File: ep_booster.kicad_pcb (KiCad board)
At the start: 2 copper layers, 45 x 21.2 mm, 31 parts, among them J1 TB002-500-04BE, J2 Conn_01x04_Pin, Q1 MMBF5457, Q2 BC849C

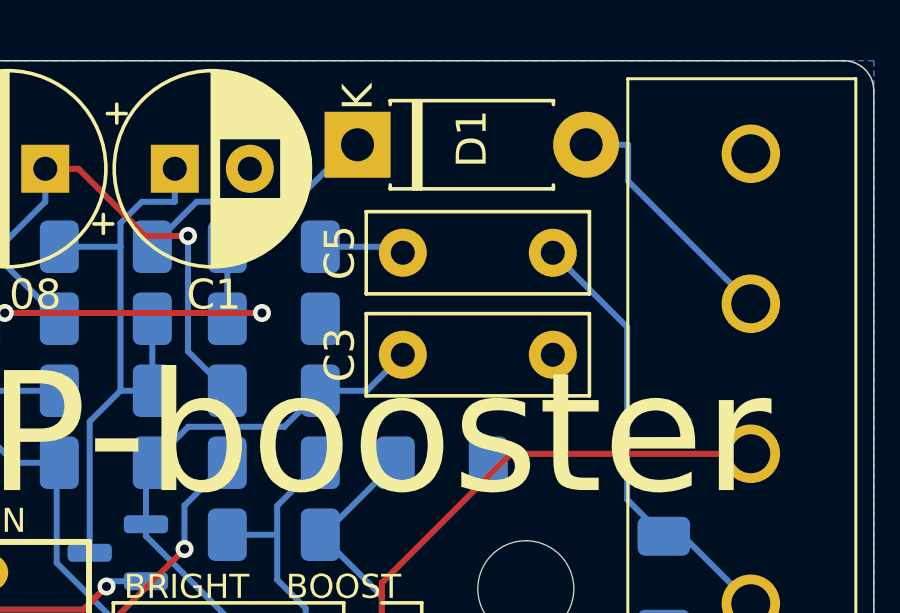
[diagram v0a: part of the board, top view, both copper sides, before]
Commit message: C5 updated footprint 2.5->3mm width
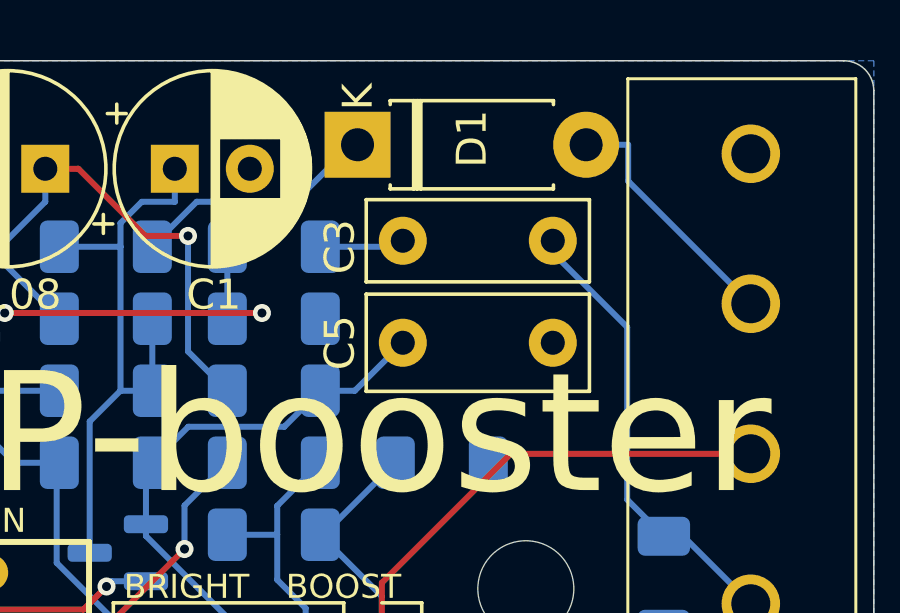
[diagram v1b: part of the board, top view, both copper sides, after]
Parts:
- C5: footprint Capacitor_THT:C_Rect_L7.2mm_W2.5mm_P5.00mm_FKS2_FKP2_MKS2_MKP2 -> Capacitor_THT:C_Rect_L7.2mm_W3.0mm_P5.00mm_FKS2_FKP2_MKS2_MKP2
- moved C5 0.40 mm to (203.9, 84.6)
- moved C3 0.40 mm to (208.9, 81.2)
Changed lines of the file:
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@@
 	(footprint "Capacitor_THT:C_Rect_L7.2mm_W2.5mm_P5.00mm_FKS2_FKP2_MKS2_MKP2"
 		(layer "F.Cu")
-		(at 208.9 81.6 180)
+		(at 208.9 81.2 180)
 		(descr "C, Rect series, Radial, pin pitch=5.00mm, , length*width=7.2*2.5mm^2, Capacitor, http://www.wima.com/EN/WIMA_FKS_2.pdf")
 		(tags "C Rect series Radial pin pitch 5.00mm  length 7.2mm width 2.5mm Capacitor")
 		(property "Reference" "C3"
-			(at 7.1 -3.4 90)
+			(at 7.1 -0.2 90)
 			(layer "F.SilkS")
 			(effects
@@
 		)
 	)
-	(footprint "Capacitor_THT:C_Rect_L7.2mm_W2.5mm_P5.00mm_FKS2_FKP2_MKS2_MKP2"
+	(footprint "Capacitor_THT:C_Rect_L7.2mm_W3.0mm_P5.00mm_FKS2_FKP2_MKS2_MKP2"
 		(layer "F.Cu")
-		(at 203.9 85)
-		(descr "C, Rect series, Radial, pin pitch=5.00mm, , length*width=7.2*2.5mm^2, Capacitor, http://www.wima.com/EN/WIMA_FKS_2.pdf")
-		(tags "C Rect series Radial pin pitch 5.00mm  length 7.2mm width 2.5mm Capacitor")
+		(at 203.9 84.6)
+		(descr "C, Rect series, Radial, pin pitch=5.00mm, , length*width=7.2*3.0mm^2, Capacitor, http://www.wima.com/EN/WIMA_FKS_2.pdf")
+		(tags "C Rect series Radial pin pitch 5.00mm  length 7.2mm width 3.0mm Capacitor")
 		(property "Reference" "C5"
-			(at -2.1 -3.4 90)
+			(at -2.1 0 90)
 			(layer "F.SilkS")
 			(effects
@@
 		)
 		(property "Value" "3n3"
-			(at 2.5 2.5 0)
+			(at 2.5 2.75 0)
 			(layer "F.Fab")
 			(effects
@@
 			)
 		)
-		(property "Footprint" "Capacitor_THT:C_Rect_L7.2mm_W2.5mm_P5.00mm_FKS2_FKP2_MKS2_MKP2"
+		(property "Footprint" "Capacitor_THT:C_Rect_L7.2mm_W3.0mm_P5.00mm_FKS2_FKP2_MKS2_MKP2"
 			(at 0 0 0)
 			(unlocked yes)
@@
 			)
 		)
+		(property "Purpose" ""
+			(at 0 0 0)
+			(unlocked yes)
+			(layer "F.Fab")
+			(hide yes)
+			(effects
+				(font
+					(size 1 1)
+					(thickness 0.15)
+				)
+			)
+		)
 		(property ki_fp_filters "C_*")
 		(sheetname "Root")
@@
 		(attr through_hole)
 		(fp_line
-			(start -1.22 -1.37)
-			(end -1.22 1.37)
+			(start -1.22 -1.62)
+			(end -1.22 1.62)
 			(stroke
 				(width 0.12)
@@
 		)
 		(fp_line
-			(start -1.22 -1.37)
-			(end 6.22 -1.37)
+			(start -1.22 -1.62)
+			(end 6.22 -1.62)
 			(stroke
 				(width 0.12)
@@
 		)
 		(fp_line
-			(start -1.22 1.37)
-			(end 6.22 1.37)
+			(start -1.22 1.62)
+			(end 6.22 1.62)
 			(stroke
 				(width 0.12)
@@
 		)
 		(fp_line
-			(start 6.22 -1.37)
-			(end 6.22 1.37)
+			(start 6.22 -1.62)
+			(end 6.22 1.62)
 			(stroke
 				(width 0.12)
@@
 		)
 		(fp_line
-			(start -1.35 -1.5)
-			(end -1.35 1.5)
+			(start -1.35 -1.75)
+			(end -1.35 1.75)
 			(stroke
 				(width 0.05)
@@
 		)
 		(fp_line
-			(start -1.35 1.5)
-			(end 6.35 1.5)
+			(start -1.35 1.75)
+			(end 6.35 1.75)
 			(stroke
 				(width 0.05)
@@
 		)
 		(fp_line
-			(start 6.35 -1.5)
-			(end -1.35 -1.5)
+			(start 6.35 -1.75)
+			(end -1.35 -1.75)
 			(stroke
 				(width 0.05)
@@
 		)
 		(fp_line
-			(start 6.35 1.5)
-			(end 6.35 -1.5)
+			(start 6.35 1.75)
+			(end 6.35 -1.75)
 			(stroke
 				(width 0.05)
@@
 		)
 		(fp_line
-			(start -1.1 -1.25)
-			(end -1.1 1.25)
+			(start -1.1 -1.5)
+			(end -1.1 1.5)
 			(stroke
 				(width 0.1)
@@
 		)
 		(fp_line
-			(start -1.1 1.25)
-			(end 6.1 1.25)
+			(start -1.1 1.5)
+			(end 6.1 1.5)
 			(stroke
 				(width 0.1)
@@
 		)
 		(fp_line
-			(start 6.1 -1.25)
-			(end -1.1 -1.25)
+			(start 6.1 -1.5)
+			(end -1.1 -1.5)
 			(stroke
 				(width 0.1)
@@
 		)
 		(fp_line
-			(start 6.1 1.25)
-			(end 6.1 -1.25)
+			(start 6.1 1.5)
+			(end 6.1 -1.5)
 			(stroke
 				(width 0.1)
@@
 			(pintype "passive")
 		)
-		(model "${KICAD8_3DMODEL_DIR}/Capacitor_THT.3dshapes/C_Rect_L7.2mm_W2.5mm_P5.00mm_FKS2_FKP2_MKS2_MKP2.wrl"
+		(model "${KICAD8_3DMODEL_DIR}/Capacitor_THT.3dshapes/C_Rect_L7.2mm_W3.0mm_P5.00mm_FKS2_FKP2_MKS2_MKP2.wrl"
 			(offset
 				(xyz 0 0 0)
@@
 	(segment
 		(start 203.7 81.4)
-		(end 203.9 81.6)
+		(end 203.9 81.2)
 		(width 0.2)
 		(layer "B.Cu")
@@
 	)
 	(segment
+		(start 211.378 84.0779)
+		(end 211.378 89.828)
+		(width 0.2)
+		(layer "B.Cu")
+		(net 4)
+	)
+	(segment
 		(start 212.6 91.05)
 		(end 213.25 91.05)
@@
 	)
 	(segment
-		(start 211.378 84.0779)
-		(end 211.378 89.828)
+		(start 208.9 81.6)
+		(end 211.3779 84.0779)
 		(width 0.2)
 		(layer "B.Cu")
@@
 	)
 	(segment
-		(start 211.3779 84.0779)
-		(end 211.378 84.0779)
+		(start 208.9 81.2)
+		(end 208.9 81.6)
 		(width 0.2)
 		(layer "B.Cu")
@@
 	)
 	(segment
-		(start 211.378 89.828)
-		(end 212.6 91.05)
+		(start 211.3779 84.0779)
+		(end 211.378 84.0779)
 		(width 0.2)
 		(layer "B.Cu")
@@
 	)
 	(segment
-		(start 208.9 81.6)
-		(end 211.3779 84.0779)
+		(start 211.378 89.828)
+		(end 212.6 91.05)
 		(width 0.2)
 		(layer "B.Cu")
@@
 	)
 	(segment
-		(start 195.3375 91.0417)
-		(end 195.3375 90.65)
+		(start 201.15 86.2)
+		(end 202.3 86.2)
 		(width 0.2)
 		(layer "B.Cu")
@@
 	)
 	(segment
-		(start 202.7 86.2)
-		(end 203.9 85)
+		(start 195.3375 91.0417)
+		(end 195.3375 90.65)
 		(width 0.2)
 		(layer "B.Cu")
@@
 	)
 	(segment
-		(start 201.15 86.2)
-		(end 202.7 86.2)
-		(width 0.2)
-		(layer "B.Cu")
-		(net 15)
-	)
-	(segment
 		(start 199.95 87.4)
 		(end 196.75 87.4)
@@
 		(width 0.2)
 		(layer "B.Cu")
+		(net 15)
+	)
+	(segment
+		(start 202.3 86.2)
+		(end 203.9 84.6)
+		(width 0.2)
+		(layer "B.Cu")

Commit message: increase track width to minimum 0.3mm, add VA and VB debug silkscreen
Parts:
- moved Q2 0.10 mm to (194.3, 91.6)
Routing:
- net GND: track 0.00 -> 6.74 mm, vias 0 -> 1
- net /BRIGHT2: track 17.2 -> 20.8 mm, vias 0 -> 1
- net Net-(Q1-D): track 12.2 -> 12.9 mm, vias 1 -> 3
- net Net-(D1-A): track 8.40 -> 7.88 mm
- net /BRIGHT1: track 11.2 -> 11.7 mm
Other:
- board text added: "VA"
- board text added: "VB"
